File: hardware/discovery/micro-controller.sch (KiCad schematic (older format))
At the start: 20 parts, among them U4 STM32F407VG, X1 CRYSTAL

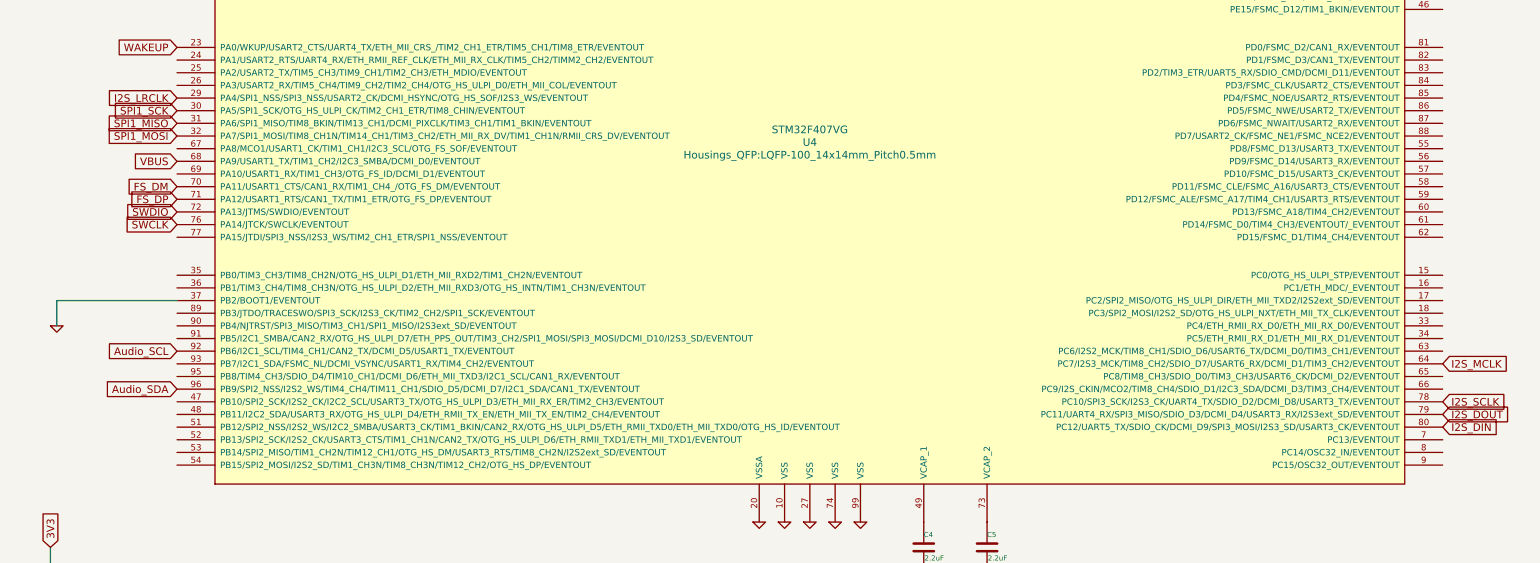
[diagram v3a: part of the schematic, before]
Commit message: Discovery: Start routing LEDs and buttons
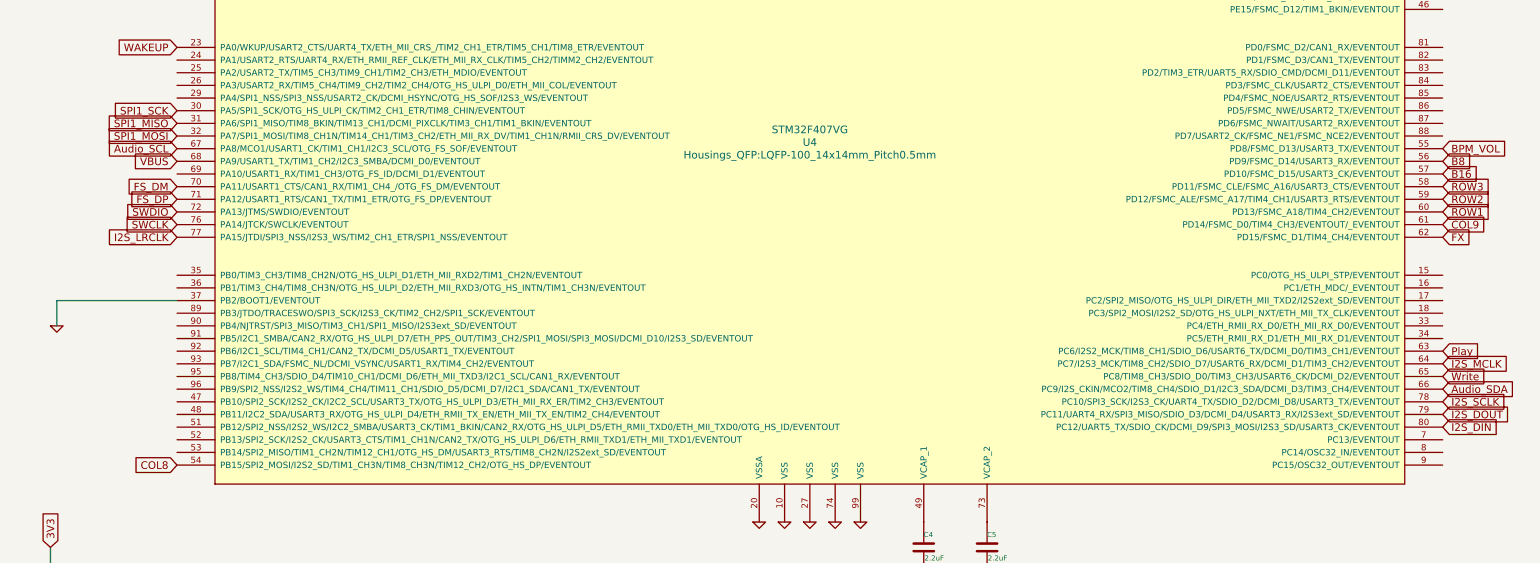
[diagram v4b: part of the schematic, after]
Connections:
- net Audio_SCL: now also U4.67 (PA8/MCO1/USART1_CK/TIM1_CH1/I2C3_SCL/OTG_FS_SOF/EVENTOUT); no longer U4.92 (PB6/I2C1_SCL/TIM4_CH1/CAN2_TX/DCMI_D5/USART1_TX/EVENTOUT)
- net Audio_SDA: now also U4.66 (PC9/I2S_CKIN/MCO2/TIM8_CH4/SDIO_D1/I2C3_SDA/DCMI_D3/TIM3_CH4/EVENTOUT); no longer U4.96 (PB9/SPI2_NSS/I2S2_WS/TIM4_CH4/TIM11_CH1/SDIO_D5/DCMI_D7/I2C1_SDA/CAN1_TX/EVENTOUT)
- net I2S_LRCLK: now also U4.77 (PA15/JTDI/SPI3_NSS/I2S3_WS/TIM2_CH1_ETR/SPI1_NSS/EVENTOUT); no longer U4.29 (PA4/SPI1_NSS/SPI3_NSS/USART2_CK/DCMI_HSYNC/OTG_HS_SOF/I2S3_WS/EVENTOUT)
- net COL8: now reaches U4.54 (PB15/SPI2_MOSI/I2S2_SD/TIM1_CH3N/TIM8_CH3N/TIM12_CH2/OTG_HS_DP/EVENTOUT)
- net BPM_VOL: now reaches U4.55 (PD8/FSMC_D13/USART3_TX/EVENTOUT)
- net B8: now reaches U4.56 (PD9/FSMC_D14/USART3_RX/EVENTOUT)
- net B16: now reaches U4.57 (PD10/FSMC_D15/USART3_CK/EVENTOUT)
- net ROW3: now reaches U4.58 (PD11/FSMC_CLE/FSMC_A16/USART3_CTS/EVENTOUT)
- net ROW2: now reaches U4.59 (PD12/FSMC_ALE/FSMC_A17/TIM4_CH1/USART3_RTS/EVENTOUT)
- net ROW1: now reaches U4.60 (PD13/FSMC_A18/TIM4_CH2/EVENTOUT)
- net COL9: now reaches U4.61 (PD14/FSMC_D0/TIM4_CH3/EVENTOUT/_EVENTOUT)
- net FX: now reaches U4.62 (PD15/FSMC_D1/TIM4_CH4/EVENTOUT)
- net Play: now reaches U4.63 (PC6/I2S2_MCK/TIM8_CH1/SDIO_D6/USART6_TX/DCMI_D0/TIM3_CH1/EVENTOUT)
- net Write: now reaches U4.65 (PC8/TIM8_CH3/SDIO_D0/TIM3_CH3/USART6_CK/DCMI_D2/EVENTOUT)
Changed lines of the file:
@@
 Comment4 ""
 $EndDescr
-Text GLabel 2850 4500 0    60   Input ~ 0
-I2S_LRCLK
 Text GLabel 2850 4600 0    60   Input ~ 0
 SPI1_SCK
@@
 Text GLabel 2850 5500 0    60   Input ~ 0
 SWCLK
-Text GLabel 2850 6500 0    60   Input ~ 0
+Text GLabel 2850 4900 0    60   Input ~ 0
 Audio_SCL
-Text GLabel 2850 6800 0    60   Input ~ 0
+Text GLabel 12850 6800 2    60   Input ~ 0
 Audio_SDA
-Text GLabel 12850 6600 2    60   Input ~ 0
-I2S_MCLK
 Text GLabel 12850 6900 2    60   Input ~ 0
 I2S_SCLK
@@
 Wire Wire Line
 	1650 8250 1650 8400
+Text GLabel 2850 5600 0    60   Input ~ 0
+I2S_LRCLK
+Text GLabel 12850 6600 2    60   Input ~ 0
+I2S_MCLK
+Text GLabel 12850 6700 2    60   Input ~ 0
+Write
+Text GLabel 12850 6500 2    60   Input ~ 0
+Play
+Text GLabel 12850 5600 2    60   Input ~ 0
+FX
+Text GLabel 12850 5500 2    60   Input ~ 0
+COL9
+Text GLabel 12850 5400 2    60   Input ~ 0
+ROW1
+Text GLabel 12850 5300 2    60   Input ~ 0
+ROW2
+Text GLabel 12850 5200 2    60   Input ~ 0
+ROW3
+Text GLabel 12850 5100 2    60   Input ~ 0
+B16
+Text GLabel 12850 5000 2    60   Input ~ 0
+B8
+Text GLabel 12850 4900 2    60   Input ~ 0
+BPM_VOL
+Text GLabel 2850 7400 0    60   Input ~ 0
+COL8
 $EndSCHEMATC

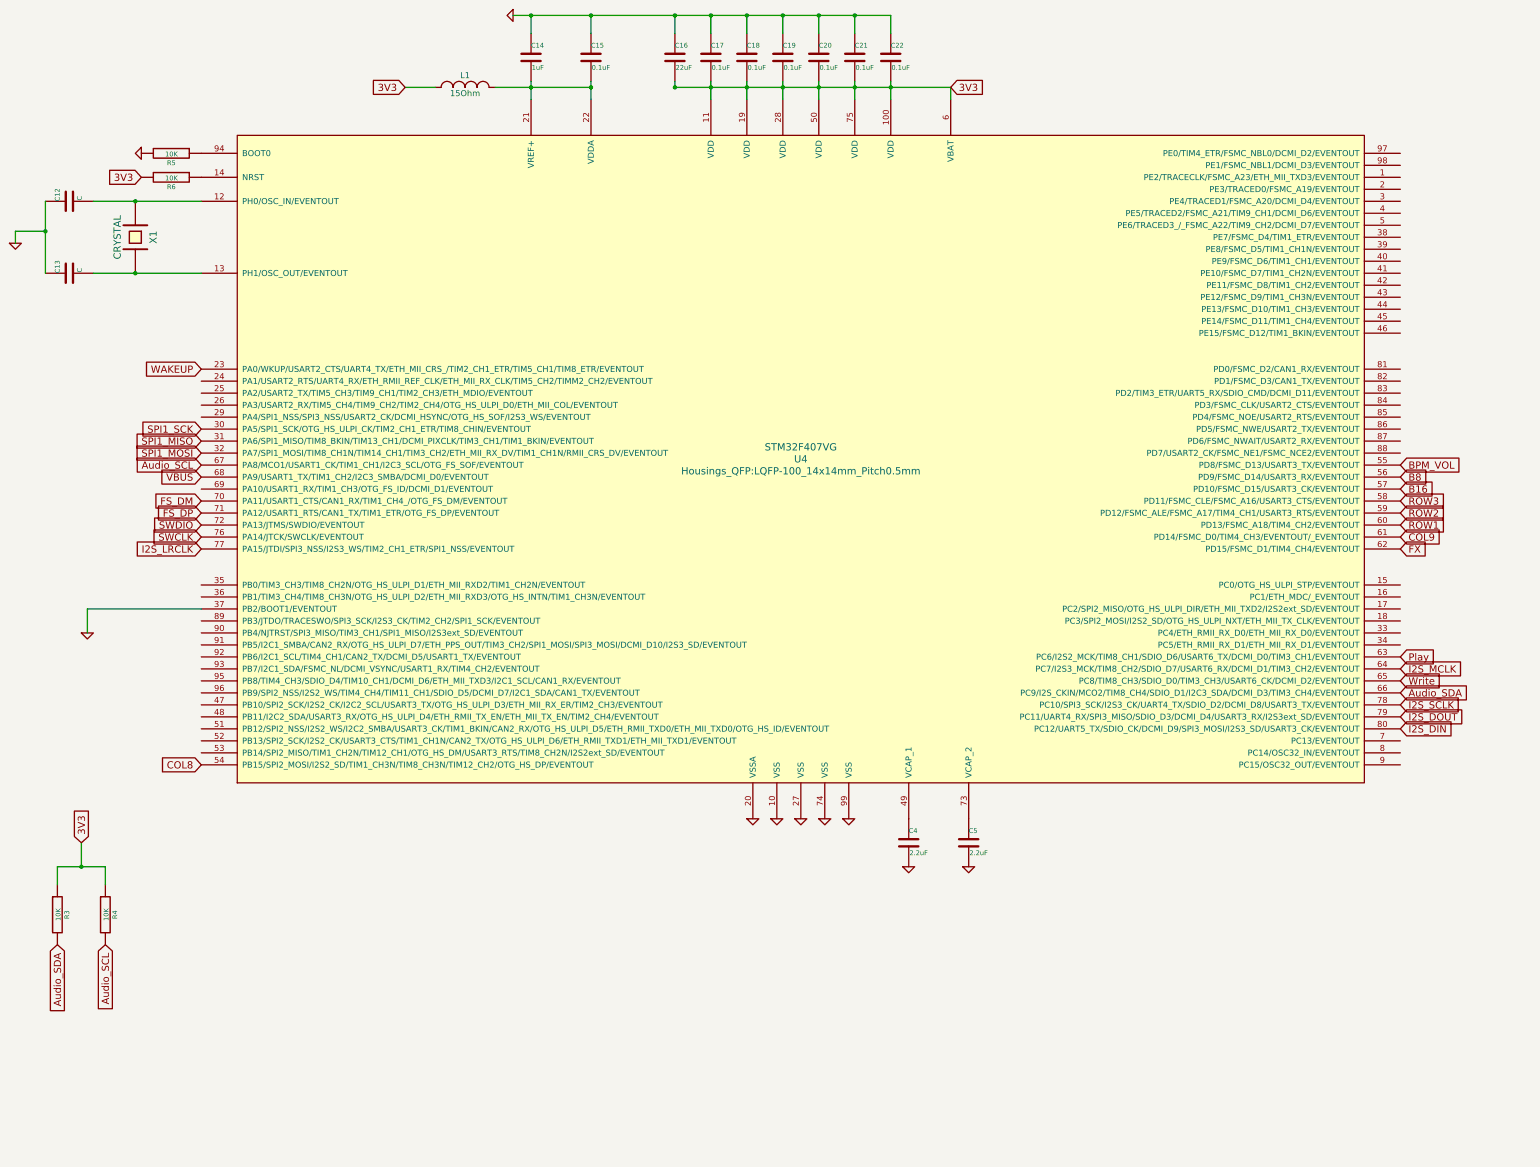
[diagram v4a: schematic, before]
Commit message: Discovery LEDs and button routing part 2
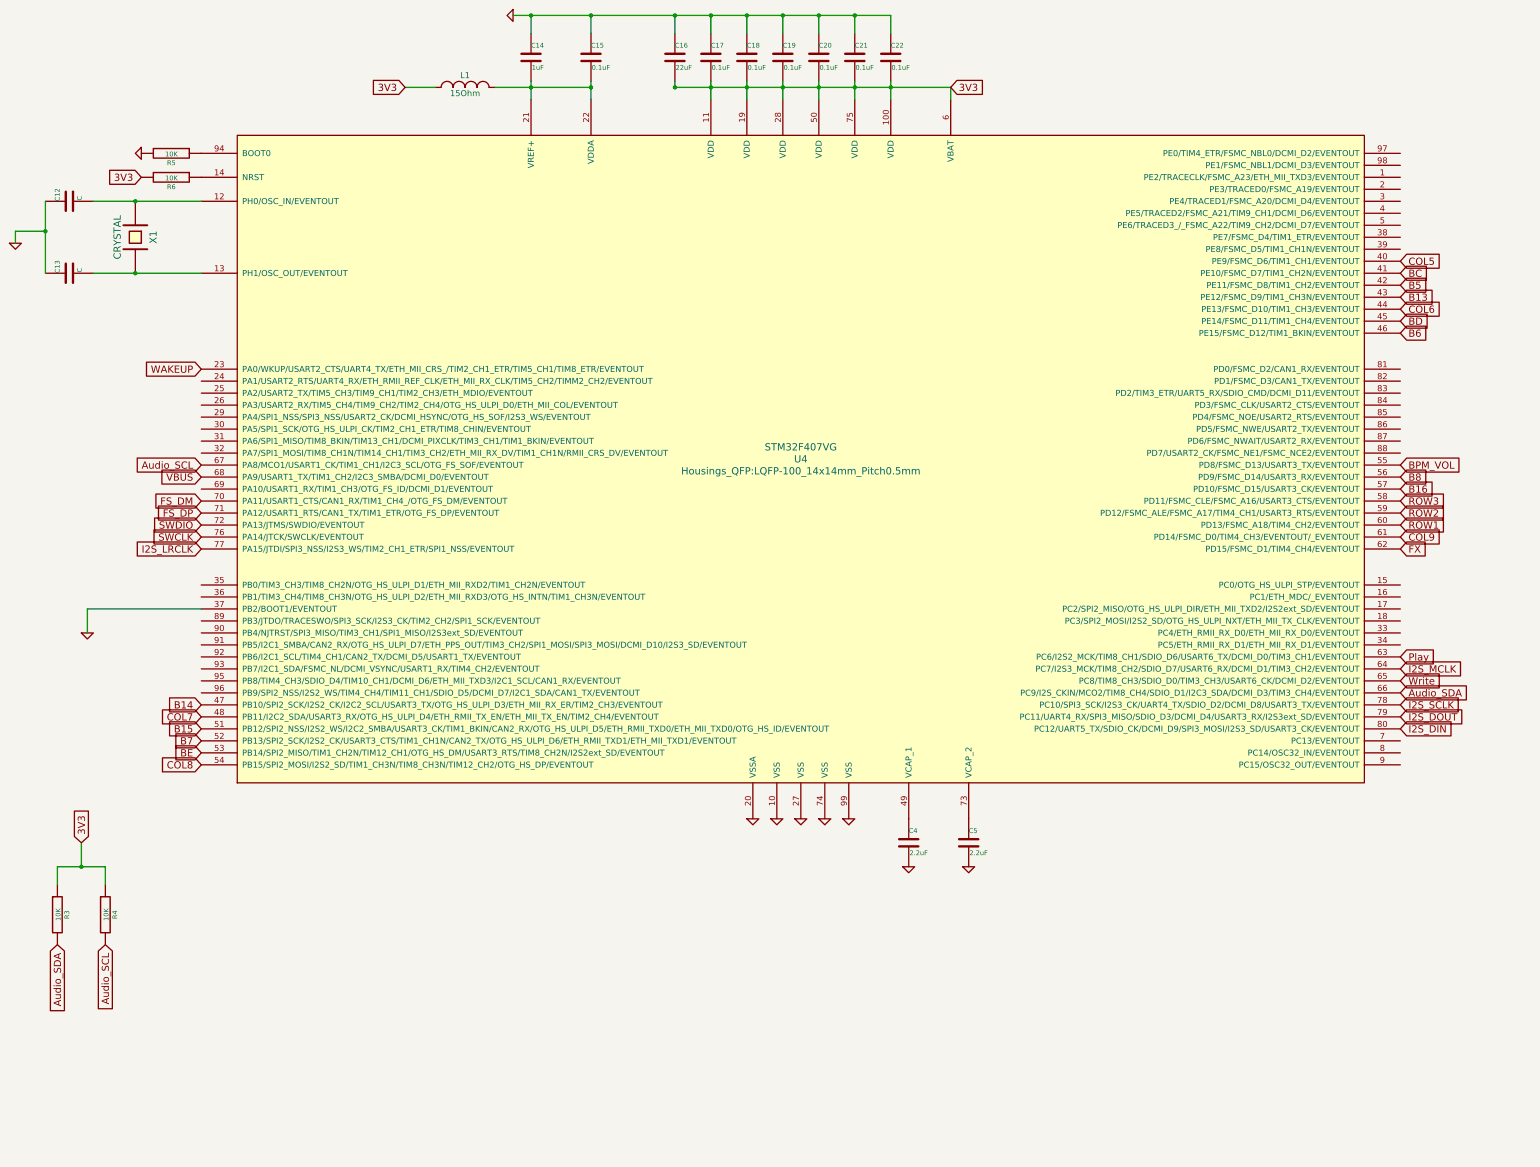
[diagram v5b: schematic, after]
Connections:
- net COL5: now reaches U4.40 (PE9/FSMC_D6/TIM1_CH1/EVENTOUT)
- net BC: now reaches U4.41 (PE10/FSMC_D7/TIM1_CH2N/EVENTOUT)
- net B5: now reaches U4.42 (PE11/FSMC_D8/TIM1_CH2/EVENTOUT)
- net B13: now reaches U4.43 (PE12/FSMC_D9/TIM1_CH3N/EVENTOUT)
- net COL6: now reaches U4.44 (PE13/FSMC_D10/TIM1_CH3/EVENTOUT)
- net BD: now reaches U4.45 (PE14/FSMC_D11/TIM1_CH4/EVENTOUT)
- net B6: now reaches U4.46 (PE15/FSMC_D12/TIM1_BKIN/EVENTOUT)
- net B14: now reaches U4.47 (PB10/SPI2_SCK/I2S2_CK/I2C2_SCL/USART3_TX/OTG_HS_ULPI_D3/ETH_MII_RX_ER/TIM2_CH3/EVENTOUT)
- net COL7: now reaches U4.48 (PB11/I2C2_SDA/USART3_RX/OTG_HS_ULPI_D4/ETH_RMII_TX_EN/ETH_MII_TX_EN/TIM2_CH4/EVENTOUT)
- net B15: now reaches U4.51 (PB12/SPI2_NSS/I2S2_WS/I2C2_SMBA/USART3_CK/TIM1_BKIN/CAN2_RX/OTG_HS_ULPI_D5/ETH_RMII_TXD0/ETH_MII_TXD0/OTG_HS_ID/EVENTOUT)
- net B7: now reaches U4.52 (PB13/SPI2_SCK/I2S2_CK/USART3_CTS/TIM1_CH1N/CAN2_TX/OTG_HS_ULPI_D6/ETH_RMII_TXD1/ETH_MII_TXD1/EVENTOUT)
- net BE: now reaches U4.53 (PB14/SPI2_MISO/TIM1_CH2N/TIM12_CH1/OTG_HS_DM/USART3_RTS/TIM8_CH2N/I2S2ext_SD/EVENTOUT)
- net SPI1_MISO: no longer names the net of U4.31 (PA6/SPI1_MISO/TIM8_BKIN/TIM13_CH1/DCMI_PIXCLK/TIM3_CH1/TIM1_BKIN/EVENTOUT)
- net SPI1_MOSI: no longer names the net of U4.32 (PA7/SPI1_MOSI/TIM8_CH1N/TIM14_CH1/TIM3_CH2/ETH_MII_RX_DV/TIM1_CH1N/RMII_CRS_DV/EVENTOUT)
- net SPI1_SCK: no longer names the net of U4.30 (PA5/SPI1_SCK/OTG_HS_ULPI_CK/TIM2_CH1_ETR/TIM8_CHIN/EVENTOUT)
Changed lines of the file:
@@
 Comment4 ""
 $EndDescr
-Text GLabel 2850 4600 0    60   Input ~ 0
-SPI1_SCK
-Text GLabel 2850 4700 0    60   Input ~ 0
-SPI1_MISO
-Text GLabel 2850 4800 0    60   Input ~ 0
-SPI1_MOSI
 Text GLabel 2850 5000 0    60   Input ~ 0
 VBUS
@@
 Text GLabel 2850 7400 0    60   Input ~ 0
 COL8
+Text GLabel 2850 7100 0    60   Input ~ 0
+B15
+Text GLabel 2850 7200 0    60   Input ~ 0
+B7
+Text GLabel 2850 7300 0    60   Input ~ 0
+BE
+Text GLabel 2850 7000 0    60   Input ~ 0
+COL7
+Text GLabel 2850 6900 0    60   Input ~ 0
+B14
+Text GLabel 12850 3800 2    60   Input ~ 0
+B6
+Text GLabel 12850 3700 2    60   Input ~ 0
+BD
+Text GLabel 12850 3600 2    60   Input ~ 0
+COL6
+Text GLabel 12850 3500 2    60   Input ~ 0
+B13
+Text GLabel 12850 3400 2    60   Input ~ 0
+B5
+Text GLabel 12850 3300 2    60   Input ~ 0
+BC
+Text GLabel 12850 3200 2    60   Input ~ 0
+COL5
 $EndSCHEMATC
